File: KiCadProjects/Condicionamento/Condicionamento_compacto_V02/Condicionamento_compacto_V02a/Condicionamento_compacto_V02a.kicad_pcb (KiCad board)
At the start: 2 copper layers, 60 x 25 mm, 28 parts, among them J2 Canais, J3 Entrada, J6 In_1 select, J7 In_2 select, U1-buffer1 AD828AN, U2-gain1 AD828AN, U3-Cond-DIP1 AD828AN, U4-Cond-SMD1 AD8056ARZ, U4-DigPot2 X9c10x, U5-DigPot1 X9c10x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

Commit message: agc
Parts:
- moved C2 1.85 mm to (124.0, 107.0), turned to 0 degrees
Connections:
- J3 pad 6: GND -> Earth
- U4-DigPot2 pad 2: GND -> Earth
- U4-DigPot2 pad 6: GND -> Earth
- U5-DigPot1 pad 2: GND -> Earth
- U5-DigPot1 pad 6: GND -> Earth
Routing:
- net Earth: track 0.00 -> 166.1 mm, vias 0 -> 12
- net Out_2: track 0.00 -> 92.7 mm, vias 0 -> 1
- net Out_1: track 0.00 -> 92.4 mm, vias 0 -> 1
- net Canal_2: track 0.00 -> 83.8 mm, vias 0 -> 1
- net +9V: track 0.00 -> 80.2 mm, vias 0 -> 2
- net -9V: track 0.00 -> 79.3 mm, vias 0 -> 3
- net Canal_1: track 0.00 -> 79.2 mm
- net Vref: track 0.00 -> 68.2 mm, vias 0 -> 1
- net Canal_2_buffer: track 0.00 -> 66.7 mm, vias 0 -> 1
- net Canal_1_gain: track 0.00 -> 62.8 mm
- net Canal_1_buffer: track 0.00 -> 57.1 mm, vias 0 -> 1
- net +5V: track 0.00 -> 43.8 mm
- net Canal_2_gain: track 0.00 -> 42.0 mm, vias 0 -> 1
- net In_gain_2: track 0.00 -> 40.2 mm
- net auxiliar_1: track 0.00 -> 37.5 mm, vias 0 -> 1
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- added copper zone on B.Cu, net Earth
- added copper zone on F.Cu, net Earth

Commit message: biblioteca analise sinal pelo osciloscopio
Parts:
- added Cf1a1: C, Capacitor_THT:CP_Radial_D5.0mm_P2.50mm, F.Cu at (69.2, 57.3)
- added Cf1b1: C, Capacitor_THT:CP_Radial_D5.0mm_P2.50mm, F.Cu at (69.2, 63.8)
- added Cf1c1: C, Capacitor_THT:CP_Radial_D5.0mm_P2.50mm, F.Cu at (69.2, 70.4)
- added Cf1d1: C, Capacitor_THT:CP_Radial_D5.0mm_P2.50mm, F.Cu at (69.2, 76.9)
- added Cf1e1: C, Capacitor_THT:CP_Radial_D5.0mm_P2.50mm, F.Cu at (69.2, 83.5)
- added Cf2a1: C, Capacitor_THT:CP_Radial_D5.0mm_P2.50mm, F.Cu at (75.8, 57.3)
- added Cf2b1: C, Capacitor_THT:CP_Radial_D5.0mm_P2.50mm, F.Cu at (75.8, 63.8)
- added Cf2c1: C, Capacitor_THT:CP_Radial_D5.0mm_P2.50mm, F.Cu at (75.8, 70.4)
- added Cf2d1: C, Capacitor_THT:CP_Radial_D5.0mm_P2.50mm, F.Cu at (75.8, 76.9)
- added Cf2e1: C, Capacitor_THT:CP_Radial_D5.0mm_P2.50mm, F.Cu at (75.8, 83.5)
- added J1: jumper cf1, Connector_PinHeader_2.54mm:PinHeader_1x02_P2.54mm_Vertical, F.Cu at (96.0, 73.7)
- added J4: jumper cf2, Connector_PinHeader_2.54mm:PinHeader_1x06_P2.54mm_Horizontal, F.Cu at (82.7, 56.3)
- added J5: in, Connector_PinSocket_2.54mm:PinSocket_1x06_P2.54mm_Horizontal, F.Cu at (91.4, 73.7)
- added J8: out, Connector_PinHeader_2.54mm:PinHeader_1x06_P2.54mm_Horizontal, F.Cu at (96.1, 56.3)

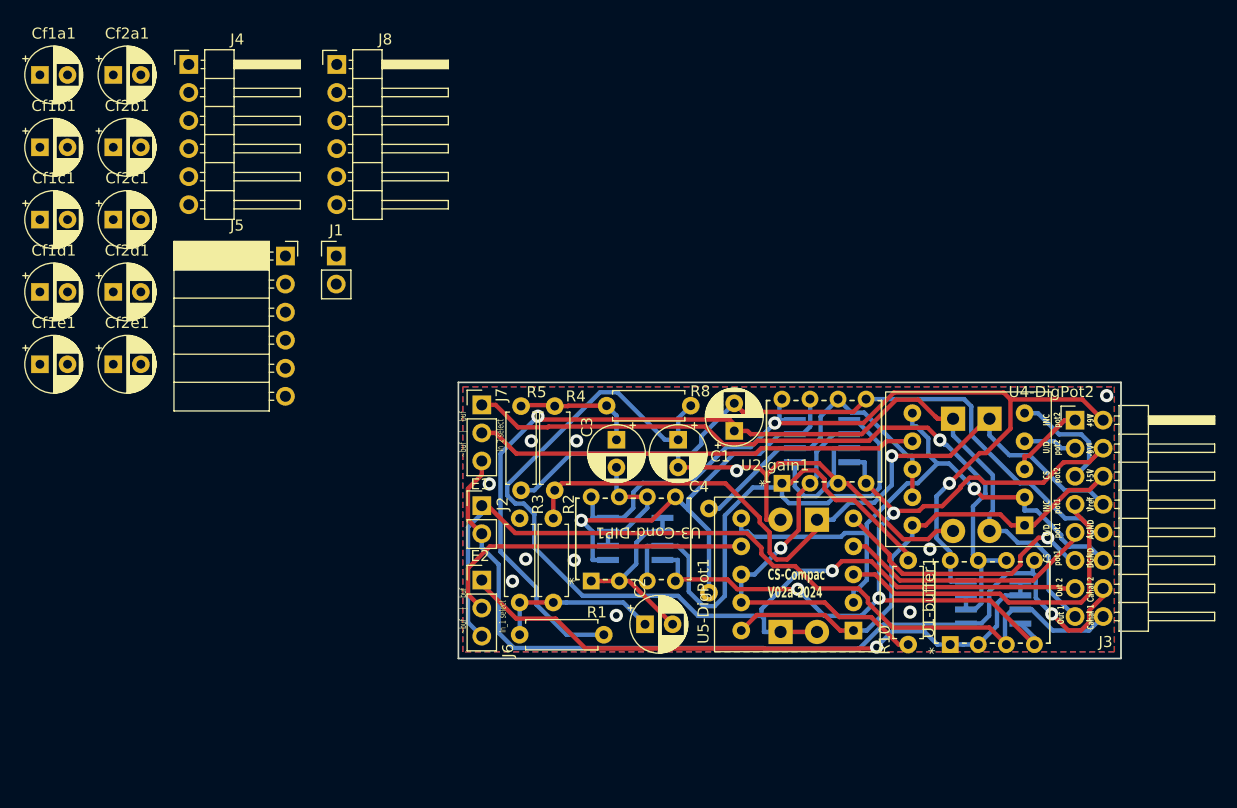
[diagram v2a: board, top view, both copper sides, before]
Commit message: versao digpot
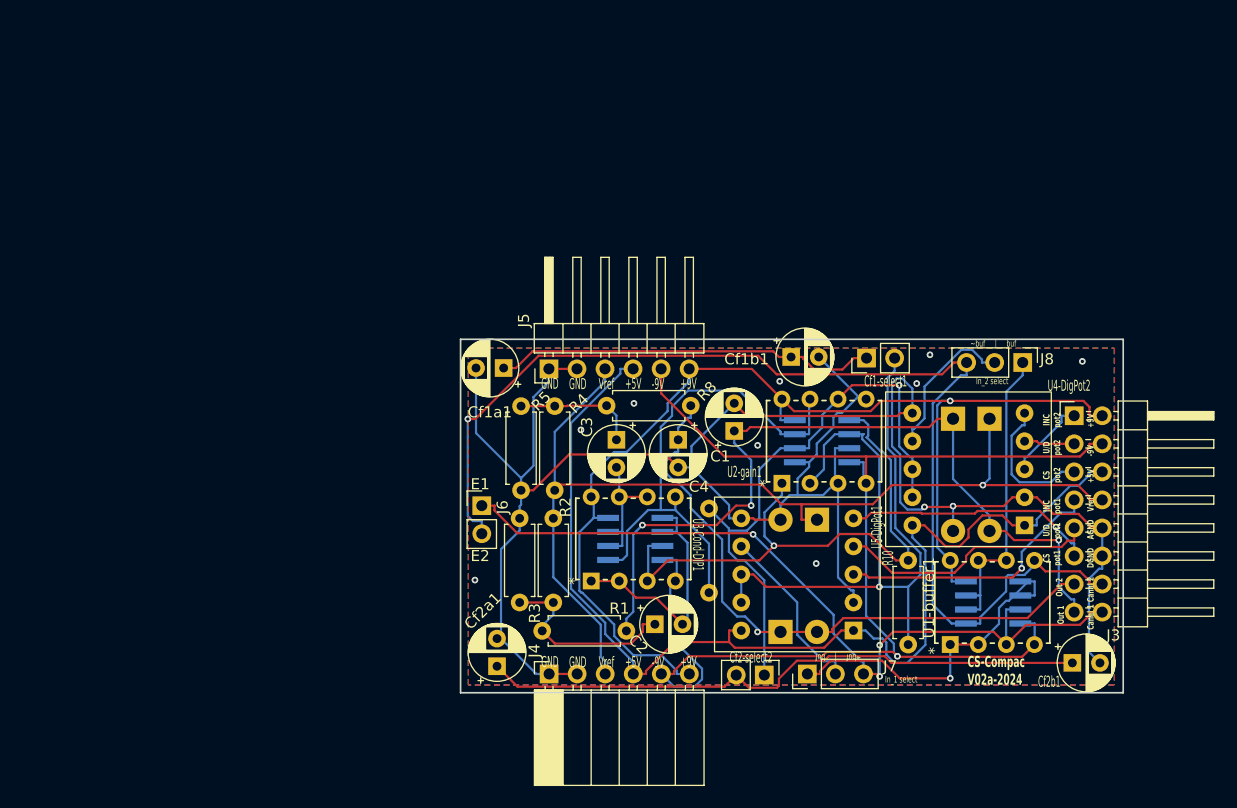
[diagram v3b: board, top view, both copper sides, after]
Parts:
- removed Cf1c1, Cf1d1, Cf1e1, Cf2c1, Cf2d1, Cf2e1: C, Capacitor_THT:CP_Radial_D5.0mm_P2.50mm
- removed the J4 at (82.7, 56.3)
- added Cf2-select2: jumper cf2, Connector_PinHeader_2.54mm:PinHeader_1x02_P2.54mm_Vertical, F.Cu at (134.8, 111.6)
- moved Cf2b1 98.6 mm to (162.7, 110.5)
- moved Cf1b1 70.6 mm to (137.2, 82.8)
- moved Cf2a1 63.8 mm to (110.6, 110.8), turned to 90 degrees
- moved Cf1a1 49.7 mm to (111.2, 83.8), turned to 180 degrees
- moved J8 49.1 mm to (158.2, 83.3), turned to -90 degrees
- moved Cf1-select1 48.9 mm to (144.1, 82.9), turned to 90 degrees
- moved J4 44.7 mm to (115.3, 111.5), turned to 90 degrees
- moved J5 33.6 mm to (115.3, 83.9), turned to 90 degrees
- moved J7 30.7 mm to (138.7, 111.5), turned to 90 degrees
- moved R1 2.07 mm to (114.7, 107.6)
- moved C2 0.89 mm to (124.9, 107.0)
- moved J3 0.41 mm to (162.9, 88.1)
- renumbered J1 to Cf1-select1, J5 to J4, J8 to J5, J2 to J6, J6 to J7, J7 to J8
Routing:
- net +5V: track 43.8 -> 100.1 mm
- net Net-(Cf2-select2-Pin_2): track 0.00 -> 56.2 mm
- net -9V: track 79.3 -> 124.3 mm, vias 3 -> 1
- net Canal_2_buffer: track 66.7 -> 28.2 mm, vias 1 -> 0
- net Out_2: track 92.7 -> 56.4 mm
- net Net-(Cf1-select1-Pin_1): track 0.00 -> 34.7 mm
- net auxiliar_1: track 37.5 -> 68.5 mm
- net Earth: track 166.1 -> 194.7 mm, vias 12 -> 11
- net In_gain_2: track 40.2 -> 13.8 mm
- net Canal_1_buffer: track 57.1 -> 31.4 mm
- net Vref: track 68.2 -> 92.5 mm
- net auxiliar_2: track 29.5 -> 52.8 mm, vias 0 -> 1
- net +9V: track 80.2 -> 103.0 mm, vias 2 -> 1
- net Canal_2: track 83.8 -> 104.4 mm
- net Out_1: track 92.4 -> 73.8 mm, vias 1 -> 3
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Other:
- board size 60 x 25 mm -> 60 x 32 mm
- board text added: "GND"
- board text removed: "In_1 select"
- board text removed: "In_2 select"
